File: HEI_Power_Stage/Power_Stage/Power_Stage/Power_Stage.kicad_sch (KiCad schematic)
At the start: 53 parts, among them IC7 AMC3311QDWERQ1, IC8 ADUM4195-1WBRIZ, J1 Screw_Terminal_01x01, J2 Conn_02x10_Odd_Even, J3 Screw_Terminal_01x01, J4 Screw_Terminal_01x01, J5 Screw_Terminal_01x01, J6 Screw_Terminal_01x01, J7 Conn_02x10_Odd_Even, U1 5V_Iso_Converter_PDSE1-S12-S5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, U16 ACS72981LLRATR-100B5

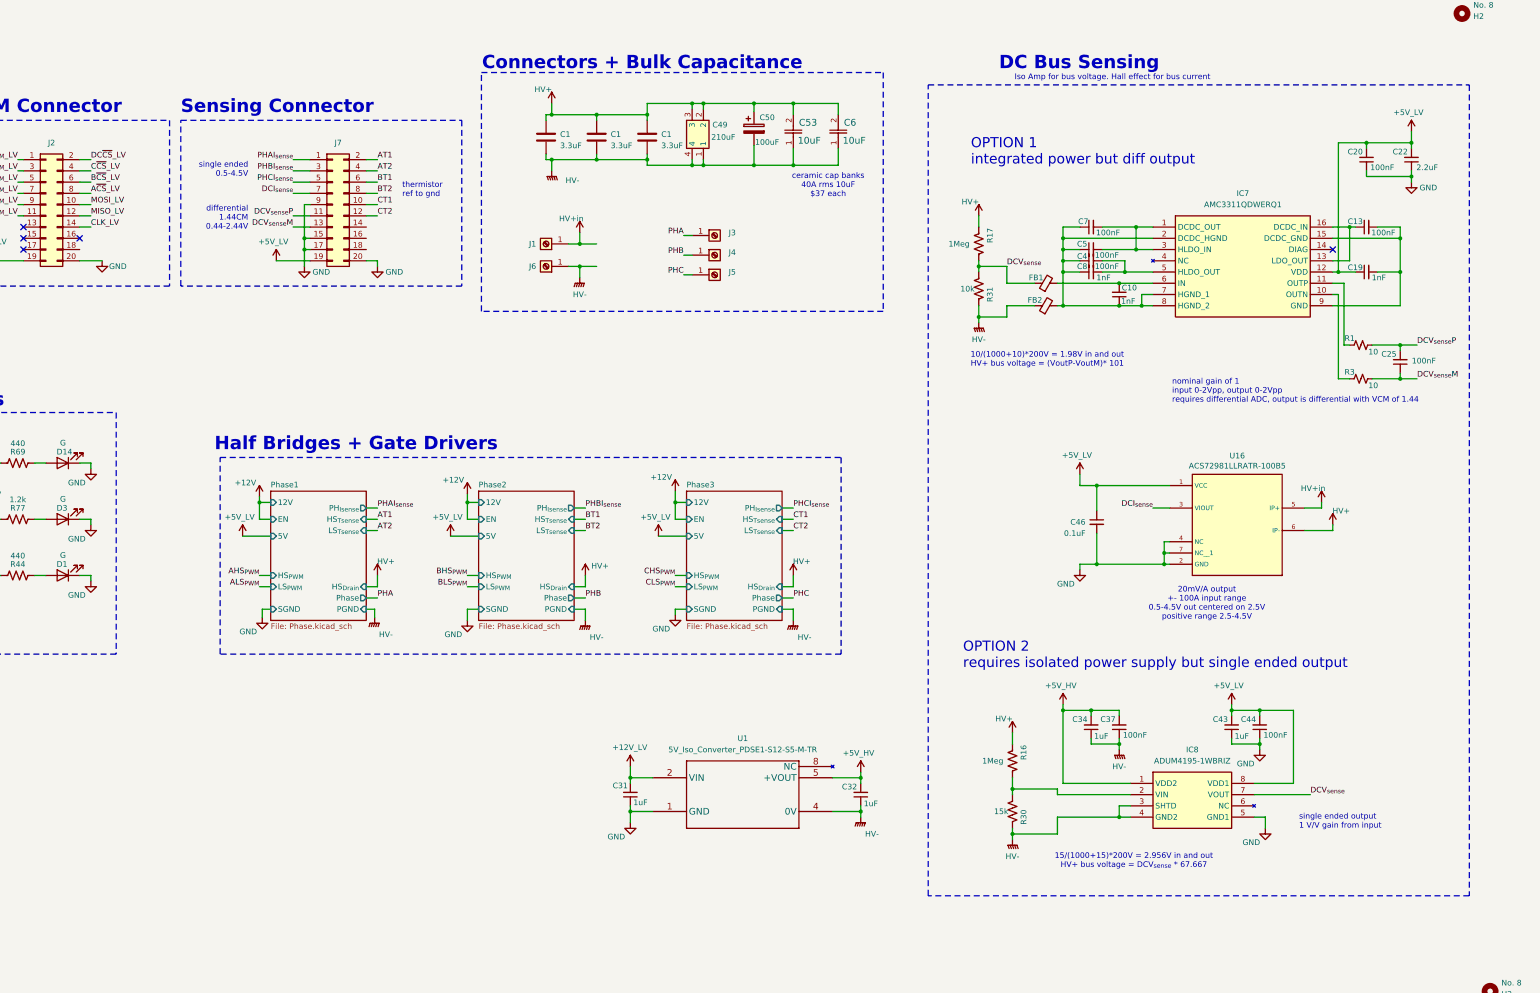
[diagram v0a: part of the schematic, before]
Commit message: I think all schematic done
added new mps gate driver, new acs current sense, new differential voltage sense, new 5-5 iso converters.
beginning layout
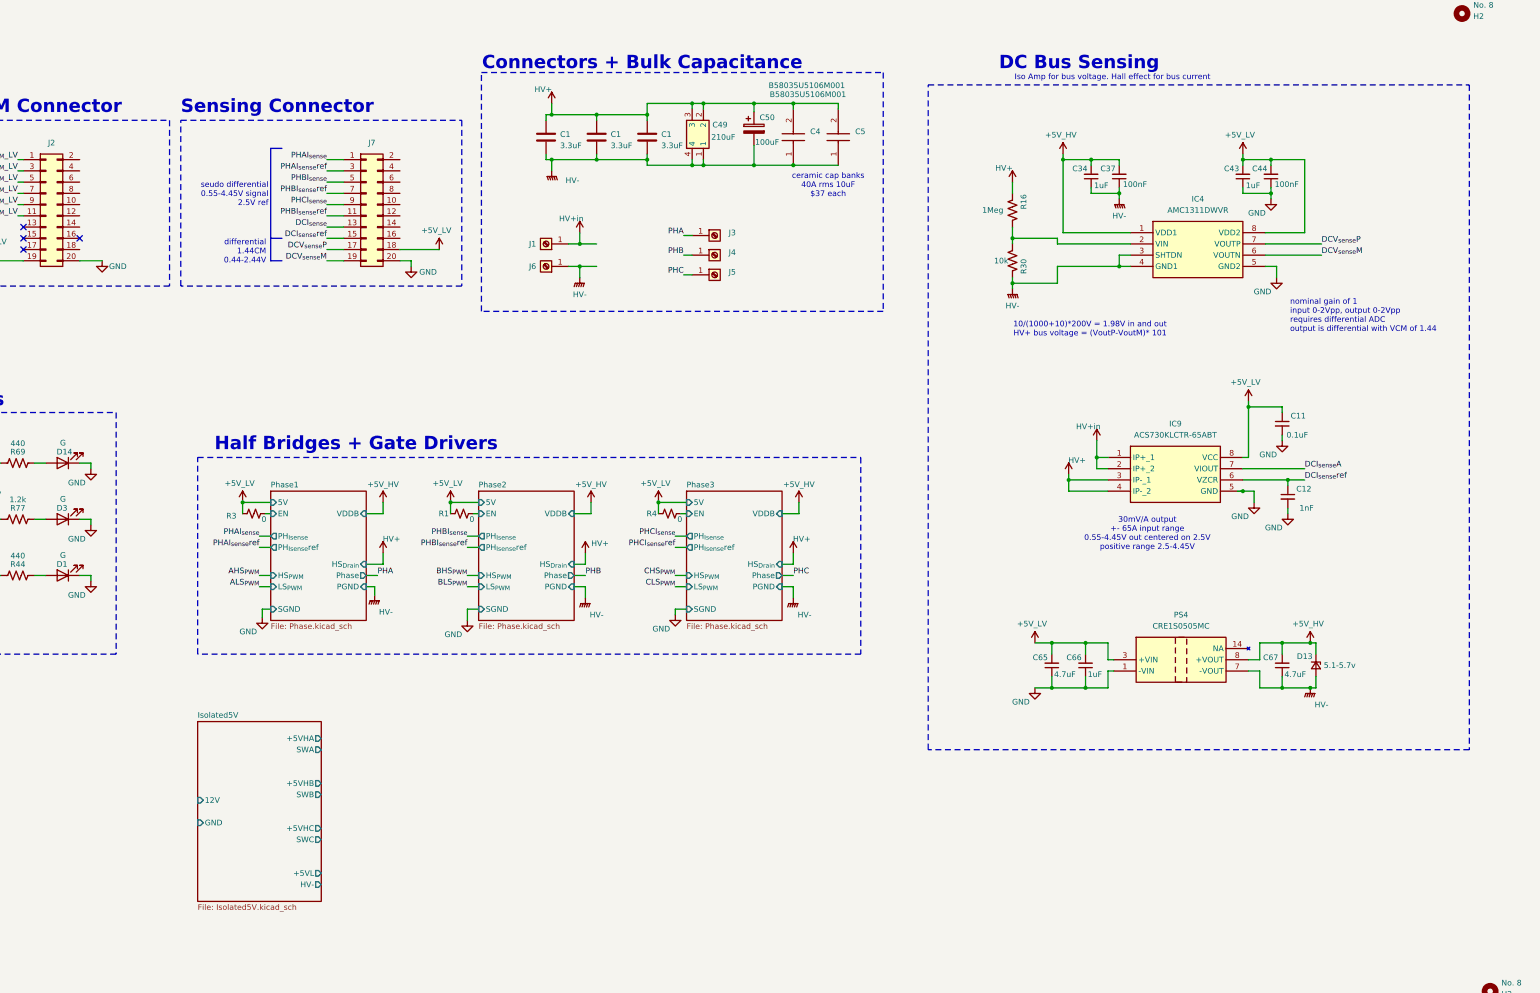
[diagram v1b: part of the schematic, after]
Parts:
- removed C10, C19, C8: 1nF, symbol Device:C_Small
- removed C13, C20, C25, C4, C5, C7: 100nF, symbol Device:C_Small
- removed C22: 2.2uF, symbol Device:C_Small
- removed C31, C32: 1uF, symbol Device:C_Small
- removed C46: 0.1uF, Capacitor_SMD:C_0603_1608Metric_Pad1.08x0.95mm_HandSolder, symbol Device:C_Small
- removed C53, C6: 10uF, CAP_B58035U-FA10_TDK, symbol long cap:B58035U5106M001
- removed FB1, FB2: ~, symbol Device:FerriteBead_Small
- removed IC7: AMC3311QDWERQ1, SOIC127P1030X265-16N, symbol AMC3311QDWERQ1:AMC3311QDWERQ1
- removed IC8: ADUM4195-1WBRIZ, SOIC127P1031X265-8N, symbol ADUM4195-1WBRIZ:ADUM4195-1WBRIZ
- removed R17: 1Meg, Resistor_SMD:R_1206_3216Metric, symbol Device:R_US
- removed R31: 10k, Resistor_SMD:R_1206_3216Metric, symbol Device:R_US
- removed U1: 5V_Iso_Converter_PDSE1-S12-S5-M-TR, GTSR_KiCAD_Footprints:PDSE1-S12-S5-M-TR, symbol GTSR_Libraries:5V_Iso_Converter_PDSE1-S12-S5-M-TR
- removed U16: ACS72981LLRATR-100B5, GTSR:XDCR_ACS72981LLRATR-100B5, symbol GTSR_symbol_lib_SD:ACS72981LLRATR-100B5
- added C11: 0.1uF, Capacitor_SMD:C_0603_1608Metric_Pad1.08x0.95mm_HandSolder, symbol Device:C_Small
- added C12: 1nF, Capacitor_SMD:C_0603_1608Metric_Pad1.08x0.95mm_HandSolder, symbol Device:C_Small
- added C4, C5: B58035U5106M001, B58035U5106M001_KiCad:B58035U5106M001, symbol B58035U5106M001:B58035U5106M001
- added C65, C67: 4.7uF, Capacitor_SMD:C_0603_1608Metric_Pad1.08x0.95mm_HandSolder, symbol Device:C_Small
- added C66: 1uF, Capacitor_SMD:C_0603_1608Metric_Pad1.08x0.95mm_HandSolder, symbol Device:C_Small
- added D13: 5.1-5.7v, Diode_SMD:D_SOD-128, symbol Device:D_Zener_Small
- added IC4: AMC1311DWVR, AMC1311_KiCad:SOIC127P1150X280-8N, symbol AMC1311DWVR:AMC1311DWVR
- added IC9: ACS730KLCTR-65ABT, ACS730KLCTR65ABT_KiCad:SOIC127P600X175-8N, symbol ACS730KLCTR-30AB-T:ACS730KLCTR-30AB-T
- added PS4: CRE1S0505MC, CRE1S0505MC_KiCad:CRE1S0505MC, symbol CRE1S0505MC:CRE1S0505MC
- added R4: 0, Resistor_SMD:R_0603_1608Metric_Pad0.98x0.95mm_HandSolder, symbol Device:R_Small_US
- C1: footprint GTSR_KiCAD_Footprints:CAP_6050_TDK -> GTSR:CAP_6050_TDK
- C34, C37, C43, C44: footprint (none) -> Capacitor_SMD:C_0603_1608Metric_Pad1.08x0.95mm_HandSolder
- C49: footprint C4AQLEW6210A3BK -> kemet_cap:C4AQLEW6210A3BK
- J3, J4, J5: footprint GTSR_KiCAD_Footprints_SD:CONN6_1057_WRE -> GTSR:CONN6_1057_WRE
- R1, R3: value 10 -> 0; footprint (none) -> Resistor_SMD:R_0603_1608Metric_Pad0.98x0.95mm_HandSolder
- R30: value 15k -> 10k
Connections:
- net +5V_HV: now also C67.2, D13.1 (K), IC4.1 (VDD1), PS4.8 (+VOUT)
- net +5V_LV: now also J7.18 (Pin_18), R1.1, R3.1, C11.1, C65.2, C66.2, IC4.8 (VDD2), IC9.8 (VCC), PS4.3 (+VIN), R4.1; no longer J7.19 (Pin_19)
- net DCI_{sense}: now also J7.13 (Pin_13); no longer J7.7 (Pin_7)
- net DCV_{sense}M: now also J7.19 (Pin_19), IC4.6 (VOUTN); no longer J7.13 (Pin_13), R3.2
- net DCV_{sense}P: now also J7.17 (Pin_17), IC4.7 (VOUTP); no longer J7.11 (Pin_11), R1.2
- net GND: now also C11.2, C12.2, C65.1, C66.1, IC4.5 (GND2), IC9.5 (GND), PS4.1 (-VIN); no longer J7.15 (Pin_15), J7.17 (Pin_17), J7.9 (Pin_9)
- net HV+: now also C4.2, C5.2, IC9.3 (IP-_1), IC9.4 (IP-_2)
- net HV+in: now also IC9.1 (IP+_1), IC9.2 (IP+_2)
- net HV-: now also C4.1, C5.1, C67.1, D13.2 (A), IC4.3 (SHTDN), IC4.4 (GND1), PS4.7 (-VOUT)
- net PHBI_{sense}: now also J7.5 (Pin_5); no longer J7.3 (Pin_3)
- net PHCI_{sense}: now also J7.9 (Pin_9); no longer J7.5 (Pin_5)
- net at R16.1, R30.2: now also IC4.2 (VIN)
- net AT1: no longer names the net of J7.2 (Pin_2)
- net AT2: no longer names the net of J7.4 (Pin_4)
- net A~{CS}_LV: no longer names the net of J2.8 (Pin_8)
- net BT1: no longer names the net of J7.6 (Pin_6)
- net BT2: no longer names the net of J7.8 (Pin_8)
- net B~{CS}_LV: no longer names the net of J2.6 (Pin_6)
- net CLK_LV: no longer names the net of J2.14 (Pin_14)
- net CT1: no longer names the net of J7.10 (Pin_10)
- net CT2: no longer names the net of J7.12 (Pin_12)
- net C~{CS}_LV: no longer names the net of J2.4 (Pin_4)
- net DC~{CS}_LV: no longer names the net of J2.2 (Pin_2)
- net MISO_LV: no longer names the net of J2.12 (Pin_12)
- net MOSI_LV: no longer names the net of J2.10 (Pin_10)
- new net DCI_{sense}A: IC9.7 (VIOUT)
- new net DCI_{sense}ref: C12.1, IC9.6 (VZCR), J7.15 (Pin_15)
- new net PHAI_{sense}ref: J7.3 (Pin_3)
- new net PHBI_{sense}ref: J7.11 (Pin_11), J7.7 (Pin_7)
- new net Phase1/EN: R3.2
- new net Phase2/EN: R1.2
- new net Phase3/EN: R4.2
- no-connect marks 5 -> 4
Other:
- added sheet Isolated5V (Isolated5V.kicad_sch)
- sheet Phase1 ports: added PH_{Isense}ref, VDDB; removed 12V, HS_{Tsense}, LS_{Tsense}
- sheet Phase2 ports: added PH_{Isense}ref, VDDB; removed 12V, HS_{Tsense}, LS_{Tsense}
- sheet Phase3 ports: added PH_{Isense}ref, VDDB; removed 12V, HS_{Tsense}, LS_{Tsense}
- note added: "30mV/A output +- 65A input range 0.55-4.45V out centered on 2.5V positive range 2.5-4.45V"
- note added: "nominal gain of 1 input 0-2Vpp, output 0-2Vpp requires differential ADC output is differential with VCM of 1.44"
- note added: "seudo differential 0.55-4.45V signal 2.5V ref"
- note removed: "15/(1000+15)*200V = 2.956V in and out HV+ bus voltage = DCV_{sense} * 67.667"
- note removed: "20mV/A output +- 100A input range 0.5-4.5V out centered on 2.5V positive range 2.5-4.5V"
- note removed: "OPTION 1 integrated power but diff output"
- note removed: "OPTION 2 requires isolated power supply but single ended output"
- note removed: "nominal gain of 1 input 0-2Vpp, output 0-2Vpp requires differential ADC, output is differential with VCM of 1.44"
- note removed: "single ended 0.5-4.5V"
- note removed: "single ended output 1 V/V gain from input"
- note removed: "thermistor ref to gnd"
- moved on the sheet: C34, C37, C43, C44, J7, R16, R30

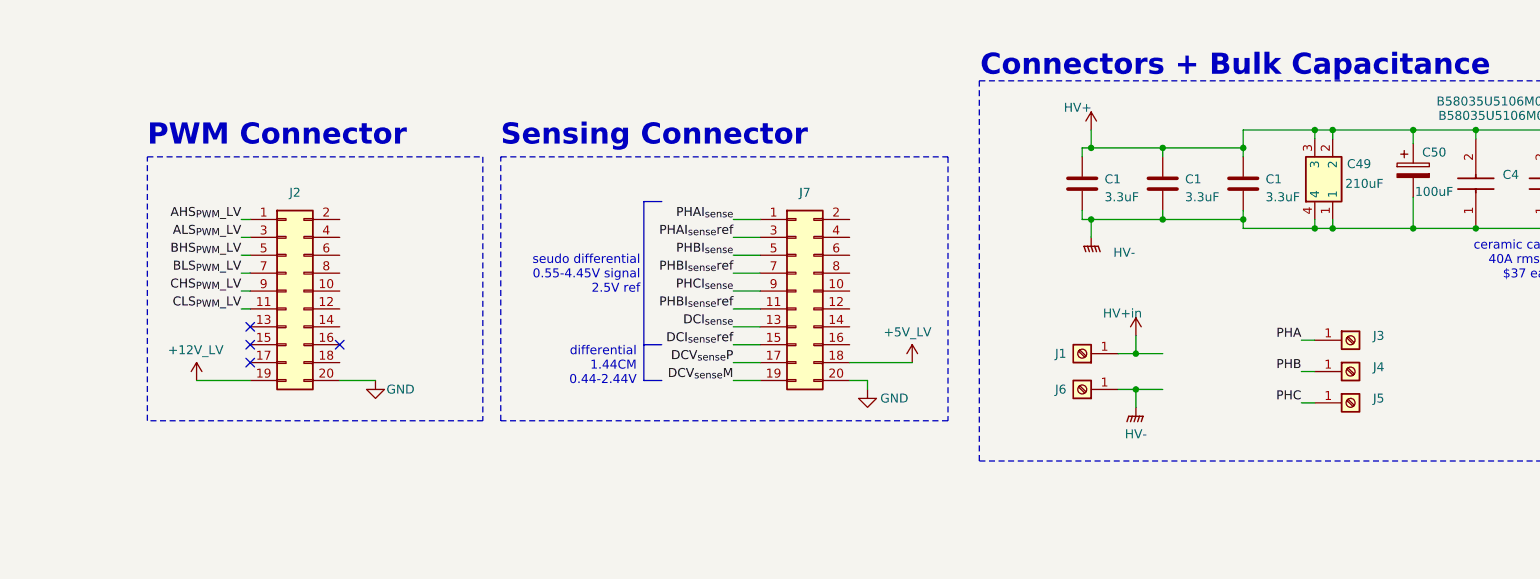
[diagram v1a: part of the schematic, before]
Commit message: more progress
started placement for each half bridge
3d bodies
connectors sorted
options for dc link cap
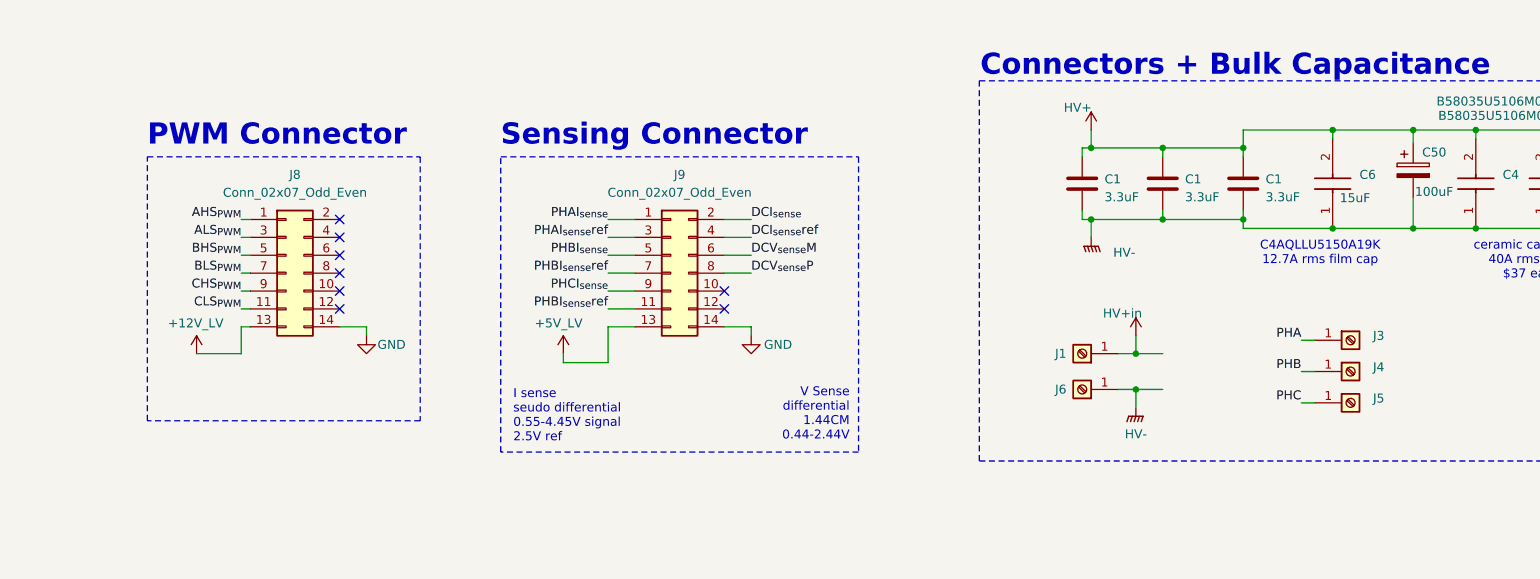
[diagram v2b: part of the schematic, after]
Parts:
- removed C49: 210uF, kemet_cap:C4AQLEW6210A3BK, symbol kemet_cap:C4AQLEW6210A3BK
- removed J2, J7: Conn_02x10_Odd_Even, Connector_PinHeader_2.54mm:PinHeader_2x10_P2.54mm_Horizontal, symbol Connector_Generic:Conn_02x10_Odd_Even
- added C6: 15uF, C4AQLLU5150A19K _KiCad:C4AQLLU5150A19K, symbol C4AQLLU5150A19K:C4AQLLU5150A19K
- added J8, J9: Conn_02x07_Odd_Even, Connector_PinSocket_2.54mm:PinSocket_2x07_P2.54mm_Vertical, symbol Connector_Generic:Conn_02x07_Odd_Even
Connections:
- net +12V_LV: now also J8.13 (Pin_13)
- net +5V_LV: now also J9.13 (Pin_13)
- net AHS_{PWM}: now also J8.1 (Pin_1)
- net ALS_{PWM}: now also J8.3 (Pin_3)
- net BHS_{PWM}: now also J8.5 (Pin_5)
- net BLS_{PWM}: now also J8.7 (Pin_7)
- net CHS_{PWM}: now also J8.9 (Pin_9)
- net CLS_{PWM}: now also J8.11 (Pin_11)
- net DCI_{sense}: now also J9.2 (Pin_2)
- net DCI_{sense}ref: now also J9.4 (Pin_4)
- net DCV_{sense}M: now also J9.6 (Pin_6)
- net DCV_{sense}P: now also J9.8 (Pin_8)
- net GND: now also J8.14 (Pin_14), J9.14 (Pin_14)
- net HV+: now also C6.2
- net HV-: now also C6.1
- net PHAI_{sense}: now also J9.1 (Pin_1)
- net PHAI_{sense}ref: now also J9.3 (Pin_3)
- net PHBI_{sense}: now also J9.5 (Pin_5)
- net PHBI_{sense}ref: now also J9.11 (Pin_11), J9.7 (Pin_7)
- net PHCI_{sense}: now also J9.9 (Pin_9)
- no-connect marks 4 -> 8
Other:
- note added: "C4AQLLU5150A19K 12.7A rms film cap"
- note added: "I sense seudo differential 0.55-4.45V signal 2.5V ref"
- note added: "V Sense differential 1.44CM 0.44-2.44V"
- note removed: "differential 1.44CM 0.44-2.44V"
- note removed: "seudo differential 0.55-4.45V signal 2.5V ref"

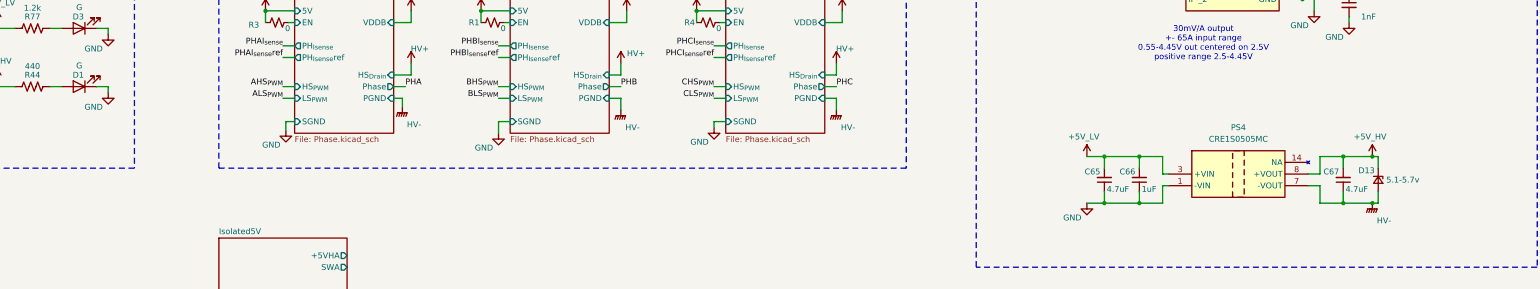
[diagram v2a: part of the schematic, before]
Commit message: placement rough draft
roughly placed all components
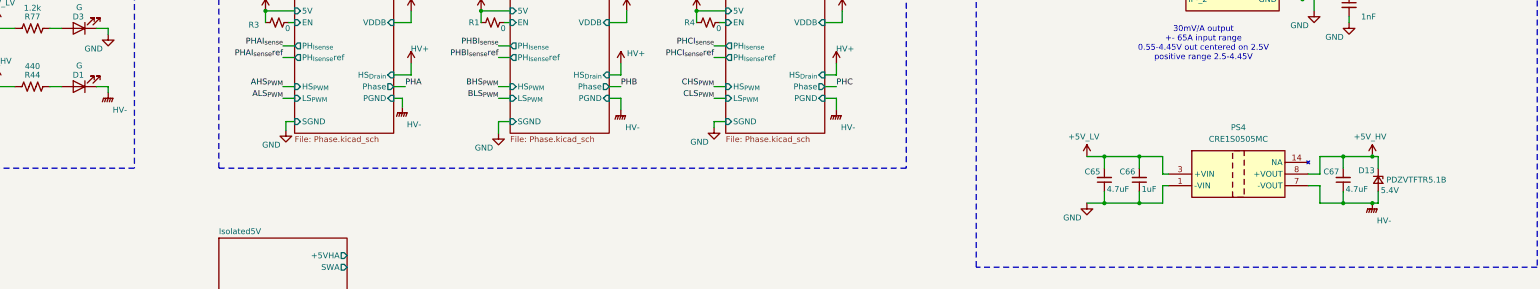
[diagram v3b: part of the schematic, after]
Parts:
- D13: value 5.1-5.7v -> PDZVTFTR5.1B; Vbreakdown (none) -> 5.4V
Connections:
- net GND: no longer D1.1 (K)
- net HV-: now also D1.1 (K)
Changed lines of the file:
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@@
 	)
 	(symbol
-		(lib_id "power:GND")
-		(at 78.74 152.4 0)
-		(unit 1)
-		(exclude_from_sim no)
-		(in_bom yes)
-		(on_board yes)
-		(dnp no)
-		(property "Reference" "#PWR047"
-			(at 78.74 158.75 0)
-			(effects
-				(font
-					(size 1.27 1.27)
-				)
-				(hide yes)
-			)
-		)
-		(property "Value" "GND"
-			(at 75.565 155.575 0)
-			(effects
-				(font
-					(size 1.27 1.27)
-				)
-			)
-		)
-		(property "Footprint" ""
-			(at 78.74 152.4 0)
-			(effects
-				(font
-					(size 1.27 1.27)
-				)
-				(hide yes)
-			)
-		)
-		(property "Datasheet" ""
-			(at 78.74 152.4 0)
-			(effects
-				(font
-					(size 1.27 1.27)
-				)
-				(hide yes)
-			)
-		)
-		(property "Description" ""
-			(at 78.74 152.4 0)
-			(effects
-				(font
-					(size 1.27 1.27)
-				)
-				(hide yes)
-			)
-		)
-		(pin "1"
-		)
-		(instances
-			(project "Power_Stage"
-				(path "/4073579f-dff4-4919-be9b-9c43467e22c1"
-					(reference "#PWR047")
-					(unit 1)
-				)
-			)
-		)
-	)
-	(symbol
 		(lib_id "power:+5V")
 		(at 55.88 76.2 0)
@@
 	)
 	(symbol
+		(lib_id "power:GNDPWR")
+		(at 78.74 152.4 0)
+		(unit 1)
+		(exclude_from_sim no)
+		(in_bom yes)
+		(on_board yes)
+		(dnp no)
+		(property "Reference" "#PWR01"
+			(at 78.74 157.48 0)
+			(effects
+				(font
+					(size 1.27 1.27)
+				)
+				(hide yes)
+			)
+		)
+		(property "Value" "HV-"
+			(at 81.28 156.21 0)
+			(effects
+				(font
+					(size 1.27 1.27)
+				)
+			)
+		)
+		(property "Footprint" ""
+			(at 78.74 153.67 0)
+			(effects
+				(font
+					(size 1.27 1.27)
+				)
+				(hide yes)
+			)
+		)
+		(property "Datasheet" ""
+			(at 78.74 153.67 0)
+			(effects
+				(font
+					(size 1.27 1.27)
+				)
+				(hide yes)
+			)
+		)
+		(property "Description" ""
+			(at 78.74 152.4 0)
+			(effects
+				(font
+					(size 1.27 1.27)
+				)
+				(hide yes)
+			)
+		)
+		(pin "1"
+		)
+		(instances
+			(project "Power_Stage"
+				(path "/4073579f-dff4-4919-be9b-9c43467e22c1"
+					(reference "#PWR01")
+					(unit 1)
+				)
+			)
+		)
+	)
+	(symbol
 		(lib_id "Device:C_Small")
 		(at 304.8 60.96 180)
@@
 			)
 		)
-		(property "Value" "5.1-5.7v"
+		(property "Value" "PDZVTFTR5.1B"
 			(at 357.378 171.45 90)
 			(effects
@@
 			)
 		)
-		(property "Datasheet" "~"
+		(property "Datasheet" "https://www.rohm.com/datasheet?p=PDZVTF5.1B&dist=Digi-key&media=referral&source=digi-key.com&campaign=Digi-key"
 			(at 355.6 171.45 90)
 			(effects
@@
 			)
 		)
-		(property "Description" "Zener diode, small symbol"
+		(property "Description" "  Zener Diode 5.4 V 1 W ±5.88% Surface Mount PMDTM"
 			(at 355.6 171.45 0)
 			(effects
@@
 			)
 		)
+		(property "Vbreakdown" "5.4V"
+			(at 358.14 173.736 90)
+			(effects
+				(font
+					(size 1.27 1.27)
+				)
+			)
+		)
